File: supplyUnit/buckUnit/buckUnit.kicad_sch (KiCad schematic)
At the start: 29 parts, among them J1 VBAT, J2 Motor, J3 Dribbler A, J4 Conn_01x05, J5 L1, J6 Conn_02x03_Counter_Clockwise, J7 Conn_02x03_Counter_Clockwise, J8 Dribbler B, J9 SPARE, Q1 BSC084P03NS3 G, Q2 IRLML6344TRPbF, SW1 SW_SPDT, U1 OKL-T6-W12P-C, U2 OKL-T6-W12P-C

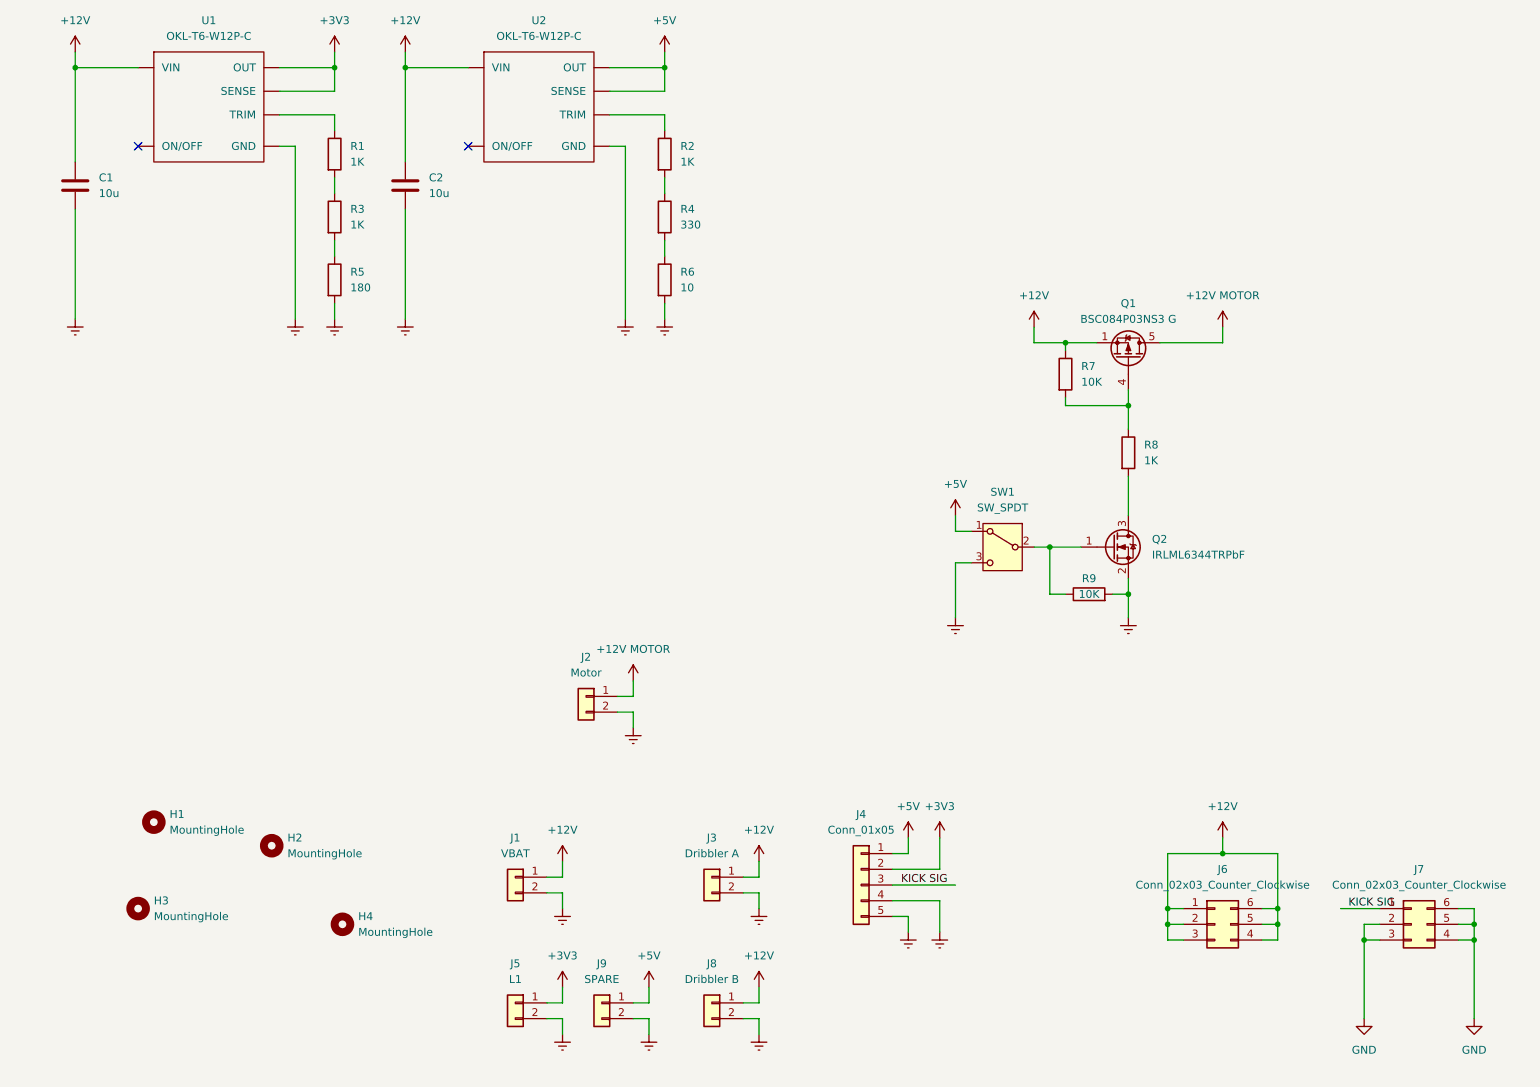
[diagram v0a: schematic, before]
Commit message: Going to move to VNH
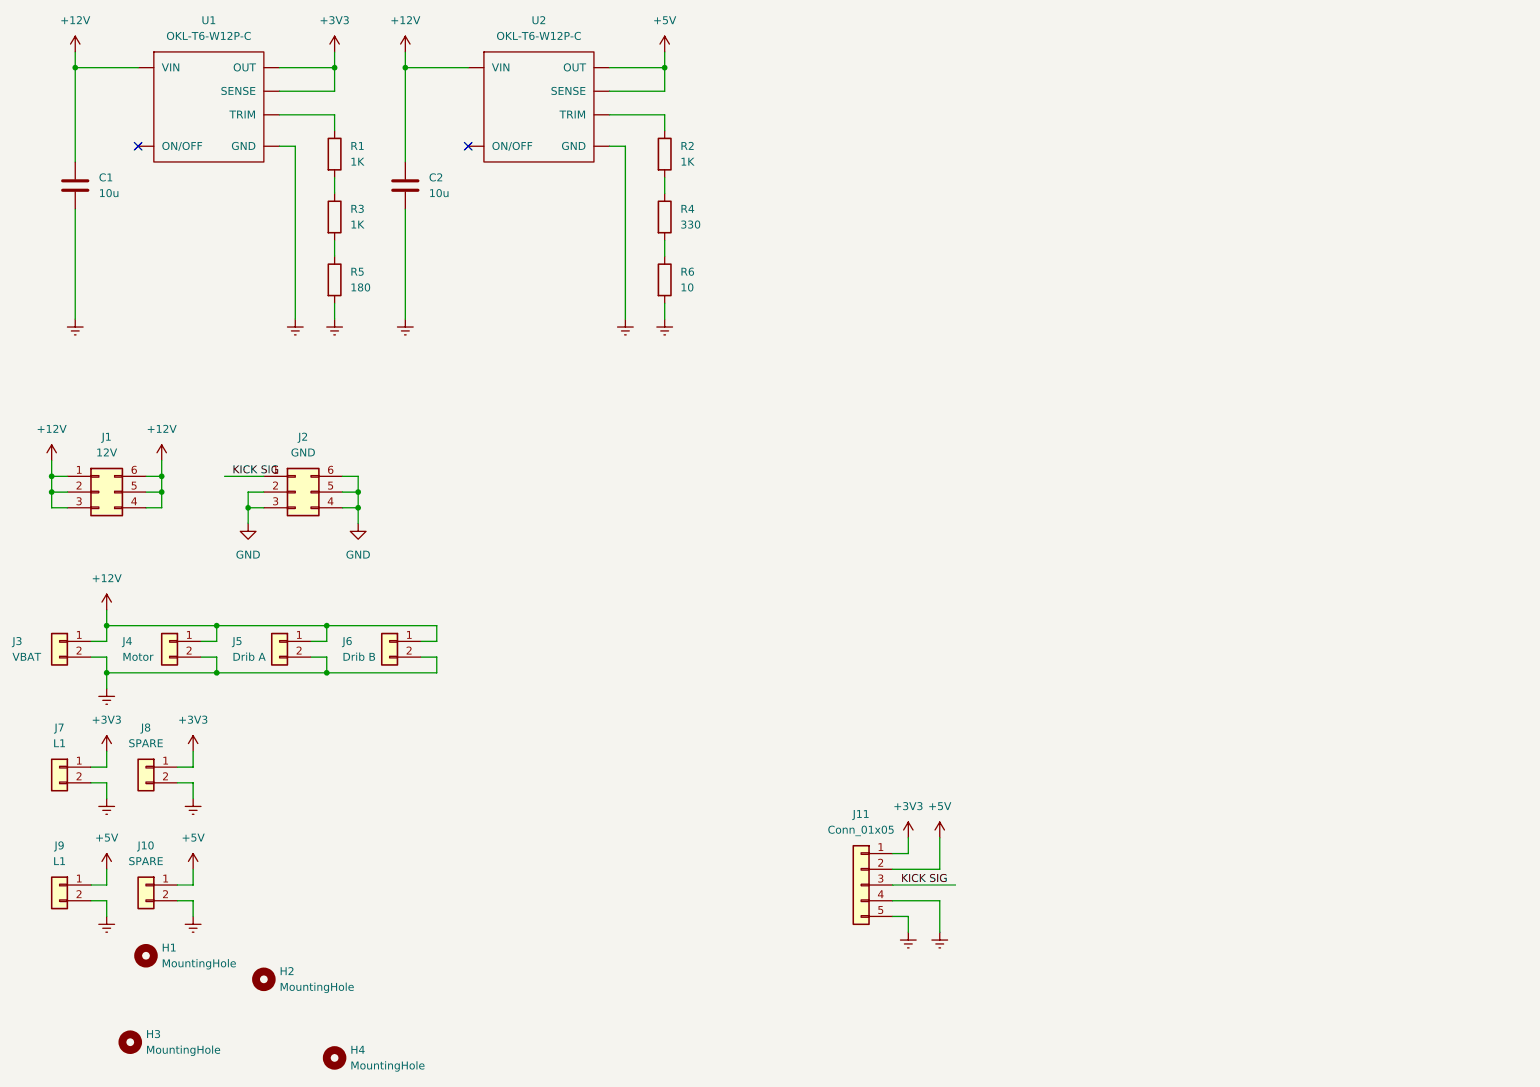
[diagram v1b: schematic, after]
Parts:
- removed J3: Dribbler A, Library:xt30-f, symbol Connector_Generic:Conn_01x02
- removed J8: Dribbler B, Library:xt30-f, symbol Connector_Generic:Conn_01x02
- removed Q1: BSC084P03NS3 G, Library:8-DFN (5x6), symbol vincent:PMOS_DGS
- removed Q2: IRLML6344TRPbF, Package_TO_SOT_SMD:SOT-23, symbol Device:Q_NMOS_GSD
- removed R7, R9: 10K, Library:res0603, symbol Device:R
- removed R8: 1K, Library:res0603, symbol Device:R
- removed SW1: SW_SPDT, Connector_PinHeader_2.54mm:PinHeader_1x03_P2.54mm_Vertical, symbol Switch:SW_SPDT
- added J10: SPARE, Connector_JST:JST_XH_B2B-XH-A_1x02_P2.50mm_Vertical, symbol Connector_Generic:Conn_01x02
- added J5: Drib A, Library:xt30-f, symbol Connector_Generic:Conn_01x02
- added J6: Drib B, Library:xt30-f, symbol Connector_Generic:Conn_01x02
- added J9: L1, Connector_JST:JST_XH_B2B-XH-A_1x02_P2.50mm_Vertical, symbol Connector_Generic:Conn_01x02
- J1: renamed from J6; value Conn_02x03_Counter_Clockwise -> 12V
- J2: renamed from J7; value Conn_02x03_Counter_Clockwise -> GND
- renumbered J4 to J11, J1 to J3, J2 to J4, J5 to J7, J9 to J8
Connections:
- net +12V MOTOR is gone; now on net +12V: J4.1 (Pin_1)
- net +12V: now also J5.1 (Pin_1), J6.1 (Pin_1)
- net +3V3: now also J11.1 (Pin_1), J8.1 (Pin_1); no longer J11.2 (Pin_2)
- net +5V: now also J11.2 (Pin_2), J10.1 (Pin_1), J9.1 (Pin_1); no longer J11.1 (Pin_1), J8.1 (Pin_1)
- net GND: now also J10.2 (Pin_2), J5.2 (Pin_2), J6.2 (Pin_2), J9.2 (Pin_2)
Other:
- moved on the sheet: H1, H2, H3, H4, J1, J2, J3, J4, J7, J8
